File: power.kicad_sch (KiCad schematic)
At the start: 1 part

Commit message: more video tracing
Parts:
- added C1: 1M250, Capacitor_THT:C_Rect_L16.5mm_W5.0mm_P15.00mm_MKT, symbol Device:C_Small
- added PL9: External Power, Connector_Dsub:DSUB-9_Male_Horizontal_P2.77x2.84mm_EdgePinOffset9.90mm_Housed_MountingHolesOffset11.32mm, symbol Connector:DE9_Plug_MountingHoles
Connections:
- net pl9_5: now reaches SW1.11 (B)
- net pl9_5: now also PL9.5
- net pl9_1: now reaches SW1.2 (B)
- net pl9_1: now also PL9.1, PL9.6
- net pl9_3: now reaches SW1.8 (B)
- net pl9_3: now also PL9.3
- new net GND: C1.1, PL9.4, PL9.8, PL9.9
- new net pl9_2: PL9.2, PL9.7, SW1.5 (B)
- no-connect marks 0 -> 5

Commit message: power tracing
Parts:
- added C2: 100nF, Capacitor_THT:C_Disc_D4.3mm_W1.9mm_P5.00mm, symbol Device:C_Small
- added C5: 220uF 35V, Capacitor_THT:CP_Axial_L25.0mm_D10.0mm_P30.00mm_Horizontal, symbol Device:C_Polarized_Small
- added C6, C9: 4700uF 16V, Capacitor_THT:CP_Axial_L34.5mm_D20.0mm_P41.00mm_Horizontal, symbol Device:C_Polarized_Small
- added D1, D2, D5, D6: 1N5401, Diode_THT:D_DO-201AD_P15.24mm_Horizontal, symbol Diode:1N5401
- added D3, D4, D7, D8: 1N4002, Diode_THT:D_DO-41_SOD81_P10.16mm_Horizontal, symbol Diode:1N4002
- added R2: 220R, Dragon:R_Axial_DIN0309_L9.0mm_D2.5mm_P12.70mm_Horizontal, symbol Device:R_Small
- added R5: 180R, Resistor_THT:R_Axial_DIN0516_L15.5mm_D5.0mm_P20.32mm_Horizontal, symbol Device:R_Small
- added REG1: LM309K, Package_TO_SOT_THT:TO-3, symbol vdg:LM309
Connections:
- net GND: now also C2.1, C5.1, C6.2, C9.2, D1.2 (A), D2.2 (A), REG1.3 (GND)
- net -5V: now reaches C1.2
- net -5V: now also R2.2
- net at SW1.10 (A): now also D4.1 (K), D8.2 (A)
- net at SW1.3 (C): now also D1.1 (K), D5.2 (A)
- net at SW1.6 (C): now also D2.1 (K), D6.2 (A)
- net at SW1.7 (A): now also D3.1 (K), D7.2 (A)
- new net: C5.2, D3.2 (A), D4.2 (A), R5.2
- new net: D7.1 (K), D8.1 (K)
- new net +5V: REG1.2 (VO)
- new net VI: C6.1, C9.1, D5.1 (K), D6.1 (K), REG1.1 (VI)
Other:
- moved on the sheet: C1, PL9

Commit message: layout and routing complete
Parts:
- added C3, C4: 1M250, Capacitor_THT:C_Rect_L16.5mm_W5.0mm_P15.00mm_MKT, symbol Device:C_Small
- added C7: 10nF, Capacitor_THT:C_Disc_D4.7mm_W2.5mm_P5.00mm, symbol Device:C_Small
- added C8: 470uF 50V, Capacitor_THT:CP_Axial_L30.0mm_D10.0mm_P35.00mm_Horizontal, symbol Device:C_Polarized_Small
- added R3, R4: 220R, Dragon:R_Axial_DIN0309_L9.0mm_D2.5mm_P12.70mm_Horizontal, symbol Device:R_Small
- added REG2: L7905, Package_TO_SOT_THT:TO-220-3_Vertical, symbol Regulator_Linear:L7905
- added REG3: LM7812_TO220, Package_TO_SOT_THT:TO-220-3_Vertical, symbol Regulator_Linear:LM7812_TO220
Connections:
- net +5V: now also C3.2, R3.1
- net -5V: now also REG2.3 (VO)
- net GND: now also R2.1, C3.1, C4.1, C7.1, C8.2, R3.2, R4.2, REG2.1 (GND), REG3.2 (GND)
- net VI: now also C2.2
- net at R5.1: now also C7.2, REG2.2 (VI)
- net at D7.1 (K), D8.1 (K): now also C8.1, REG3.1 (VI)
- new net +12V: C4.2, R4.1, REG3.3 (VO)
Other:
- moved on the sheet: C1, R2

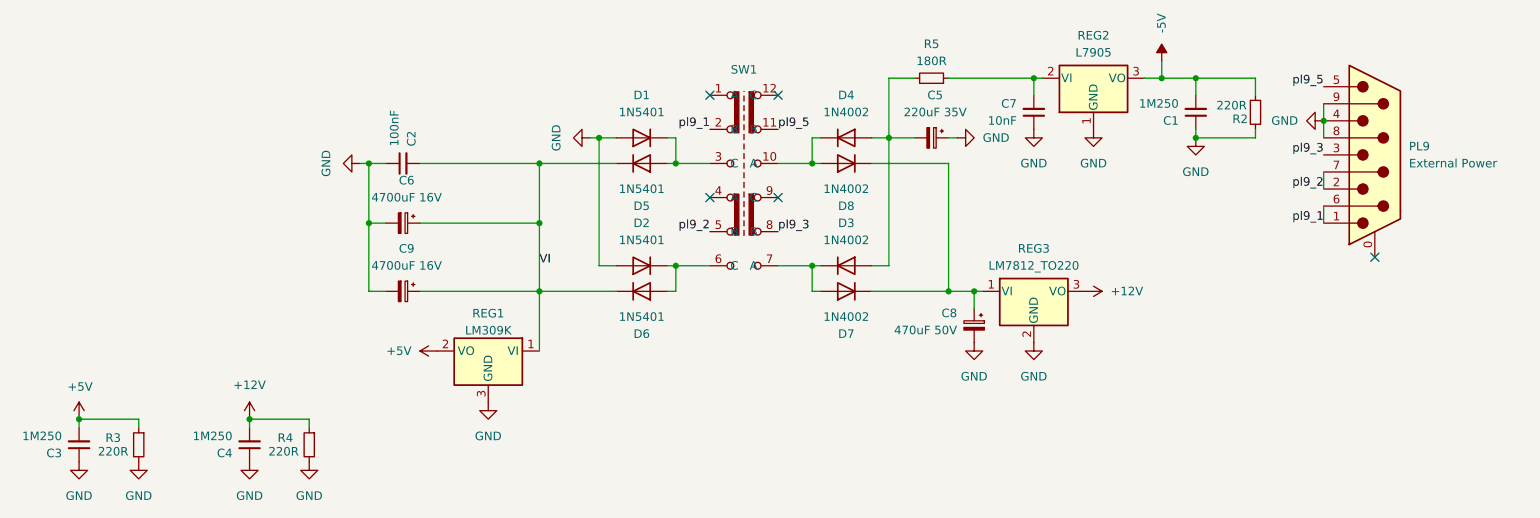
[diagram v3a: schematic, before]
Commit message: rationalise rgb circuit
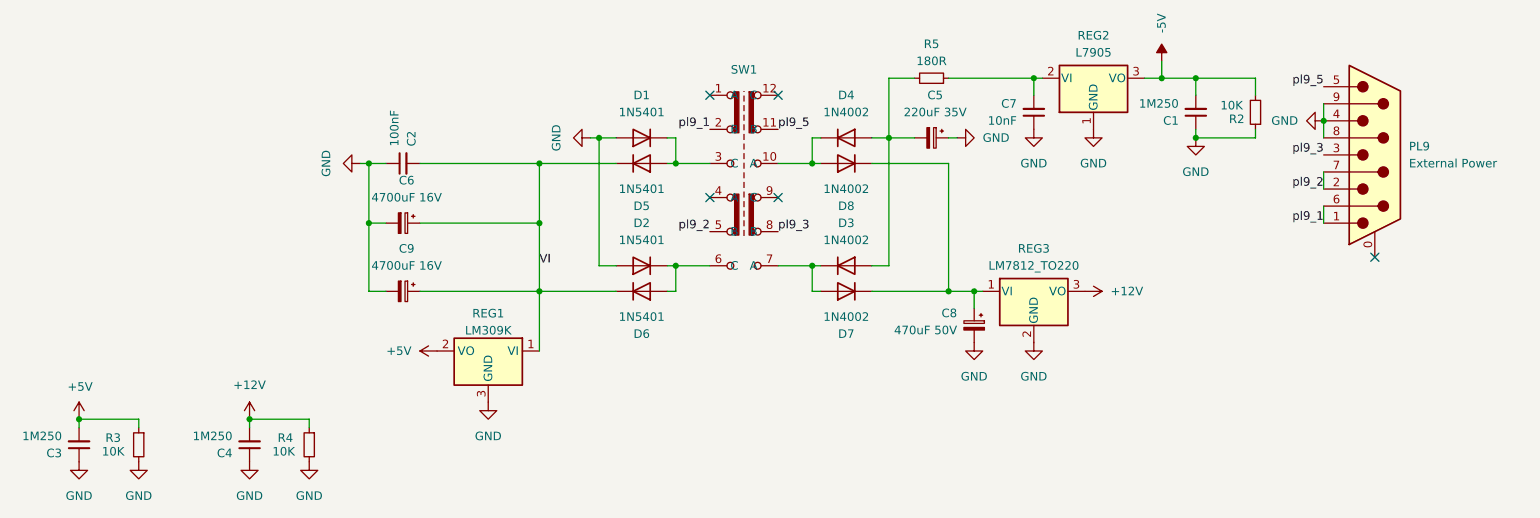
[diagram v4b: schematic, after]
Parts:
- R2, R3, R4: value 220R -> 10K
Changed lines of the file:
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@@
 		(dnp no)
 		(property "Reference" "R2"
-			(at 203.454 41.656 0)
-			(effects
-				(font
-					(size 1.27 1.27)
-				)
-			)
-		)
-		(property "Value" "220R"
+			(at 202.946 41.656 0)
+			(effects
+				(font
+					(size 1.27 1.27)
+				)
+			)
+		)
+		(property "Value" "10K"
 			(at 202.184 39.624 0)
 			(effects
@@
 			)
 		)
-		(property "Value" "220R"
+		(property "Value" "10K"
 			(at 35.56 91.186 0)
 			(effects
@@
 			)
 		)
-		(property "Value" "220R"
+		(property "Value" "10K"
 			(at 60.96 91.186 0)
 			(effects
